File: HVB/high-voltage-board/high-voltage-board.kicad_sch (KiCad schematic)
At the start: 18 parts, among them J1 Conn_01x23, J11 HV-, J2 HECS, J3 HV+, J4 HV-, J5 HV+, J6 HV-, J7 Conn_01x02, J8 HV+, J9 Bender-LV

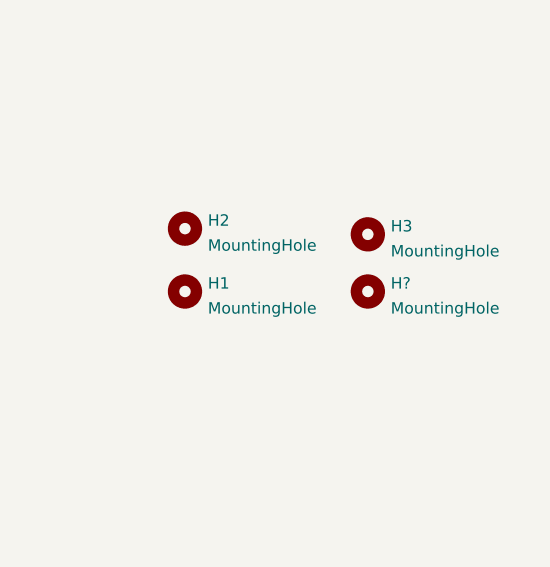
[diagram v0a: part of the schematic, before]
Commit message: adding mounting holes
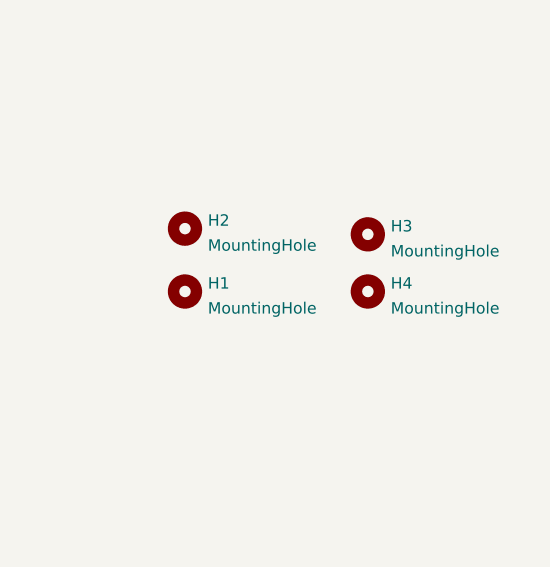
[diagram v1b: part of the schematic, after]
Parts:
- gave numbers to parts that had none: 1
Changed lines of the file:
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@@
   (symbol (lib_id "Mechanical:MountingHole") (at 262.255 162.56 0) (unit 1)
     (in_bom yes) (on_board yes) (fields_autoplaced)
-    (property "Reference" "H?" (id 0) (at 264.795 161.6515 0)
+    (property "Reference" "H4" (id 0) (at 264.795 161.6515 0)
       (effects (font (size 1.27 1.27)) (justify left))
     )
@@
     )
     (path "/245952d0-0e97-4e26-9005-0024054bd321"
-      (reference "H?") (unit 1) (value "MountingHole") (footprint "MountingHole:MountingHole_3.2mm_M3")
+      (reference "H4") (unit 1) (value "MountingHole") (footprint "MountingHole:MountingHole_3.2mm_M3")
     )
     (path "/00000000-0000-0000-0000-00005c830583"

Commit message: updating footprint and 3d model links
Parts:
- J1: footprint AERO_Footprints:TE_1-776087-1 -> AERO_Footprints:TE_1-770669-1_23pin_Horizontal
- J5, J6: footprint Connector_TE-Connectivity:TE_MATE-N-LOK_1-770870-x_1x03_P4.14mm_Vertical -> AERO_Footprints:TE_MATE-N-LOK_1-770870-x_1x03_P4.14mm_Vertical
- J7: footprint Connector_JST:JST_PH_B2B-PH-K_1x02_P2.00mm_Vertical -> Connector_JST:JST_XH_B2B-XH-A_1x02_P2.50mm_Vertical
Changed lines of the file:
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@@
     (property "Reference" "J1" (id 0) (at 23.622 132.9182 0))
     (property "Value" "Conn_01x23" (id 1) (at 23.622 135.2296 0))
-    (property "Footprint" "AERO_Footprints:TE_1-776087-1" (id 2) (at 21.59 166.37 0)
+    (property "Footprint" "AERO_Footprints:TE_1-770669-1_23pin_Horizontal" (id 2) (at 21.59 166.37 0)
       (effects (font (size 1.27 1.27)) hide)
     )
@@
       (effects (font (size 1.27 1.27)) (justify right))
     )
-    (property "Footprint" "Connector_TE-Connectivity:TE_MATE-N-LOK_1-770870-x_1x03_P4.14mm_Vertical" (id 2) (at 45.72 31.75 0)
+    (property "Footprint" "AERO_Footprints:TE_MATE-N-LOK_1-770870-x_1x03_P4.14mm_Vertical" (id 2) (at 45.72 31.75 0)
       (effects (font (size 1.27 1.27)) hide)
     )
@@
     (property "Reference" "J6" (id 0) (at 51.435 48.26 90))
     (property "Value" "HV-" (id 1) (at 52.07 45.72 90))
-    (property "Footprint" "Connector_TE-Connectivity:TE_MATE-N-LOK_1-770870-x_1x03_P4.14mm_Vertical" (id 2) (at 45.72 48.26 0)
+    (property "Footprint" "AERO_Footprints:TE_MATE-N-LOK_1-770870-x_1x03_P4.14mm_Vertical" (id 2) (at 45.72 48.26 0)
       (effects (font (size 1.27 1.27)) hide)
     )
@@
     (property "Reference" "J7" (id 0) (at 67.945 185.8985 0))
     (property "Value" "Conn_01x02" (id 1) (at 67.945 188.6736 0))
-    (property "Footprint" "Connector_JST:JST_PH_B2B-PH-K_1x02_P2.00mm_Vertical" (id 2) (at 67.945 193.675 0)
+    (property "Footprint" "Connector_JST:JST_XH_B2B-XH-A_1x02_P2.50mm_Vertical" (id 2) (at 67.945 193.675 0)
       (effects (font (size 1.27 1.27)) hide)
     )
@@
     )
     (path "/00000000-0000-0000-0000-00005c830583"
-      (reference "J1") (unit 1) (value "Conn_01x23") (footprint "AERO_Footprints:TE_1-776087-1")
+      (reference "J1") (unit 1) (value "Conn_01x23") (footprint "AERO_Footprints:TE_1-770669-1_23pin_Horizontal")
     )
     (path "/00000000-0000-0000-0000-00005c830507"
@@
     )
     (path "/00000000-0000-0000-0000-00005c8305f3"
-      (reference "J5") (unit 1) (value "HV+") (footprint "Connector_TE-Connectivity:TE_MATE-N-LOK_1-770870-x_1x03_P4.14mm_Vertical")
+      (reference "J5") (unit 1) (value "HV+") (footprint "AERO_Footprints:TE_MATE-N-LOK_1-770870-x_1x03_P4.14mm_Vertical")
     )
     (path "/00000000-0000-0000-0000-00005c830602"
-      (reference "J6") (unit 1) (value "HV-") (footprint "Connector_TE-Connectivity:TE_MATE-N-LOK_1-770870-x_1x03_P4.14mm_Vertical")
+      (reference "J6") (unit 1) (value "HV-") (footprint "AERO_Footprints:TE_MATE-N-LOK_1-770870-x_1x03_P4.14mm_Vertical")
     )
     (path "/980ee780-2ccd-48d0-81e9-943616a2d3fc"
-      (reference "J7") (unit 1) (value "Conn_01x02") (footprint "Connector_JST:JST_PH_B2B-PH-K_1x02_P2.00mm_Vertical")
+      (reference "J7") (unit 1) (value "Conn_01x02") (footprint "Connector_JST:JST_XH_B2B-XH-A_1x02_P2.50mm_Vertical")
     )
     (path "/14999d0e-4e0c-4ec9-a7cb-88c272b22a6c"

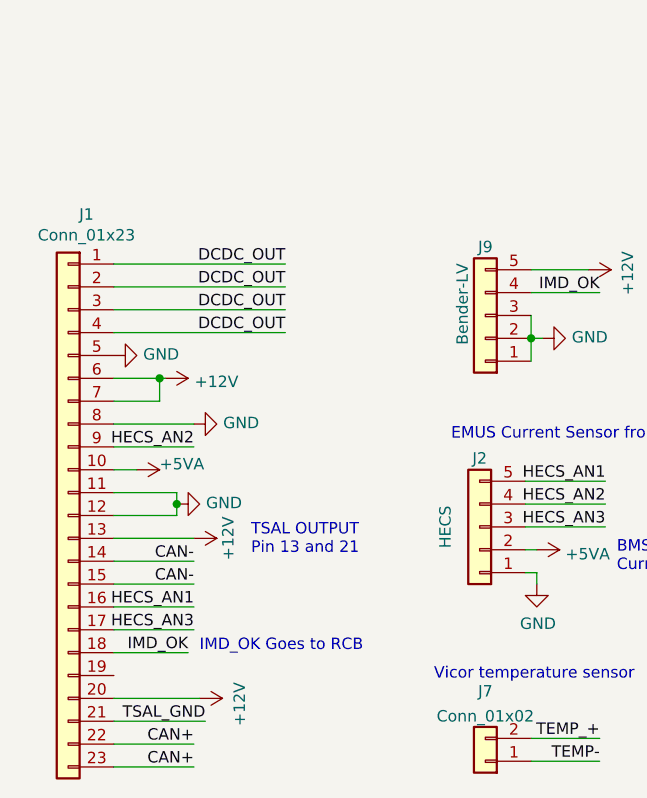
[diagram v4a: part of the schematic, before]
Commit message: updating can pinouts
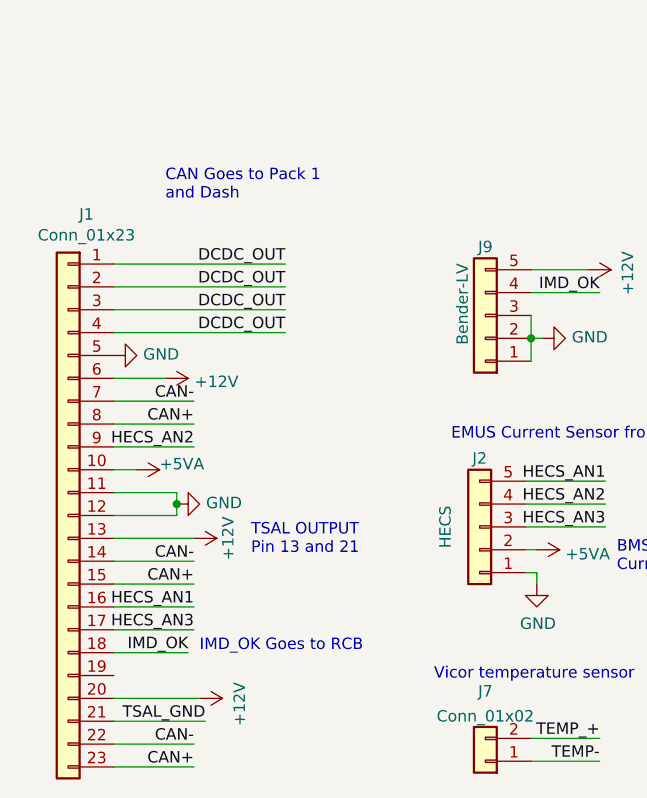
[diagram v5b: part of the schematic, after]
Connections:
- net +12V: no longer J1.7 (Pin_7)
- net CAN+: now also J1.15 (Pin_15), J1.8 (Pin_8); no longer J1.22 (Pin_22)
- net CAN-: now also J1.22 (Pin_22), J1.7 (Pin_7); no longer J1.15 (Pin_15)
- net GND: no longer J1.8 (Pin_8)
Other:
- note added: "CAN Goes to Pack 1 and Dash"
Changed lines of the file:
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@@
   (junction (at 45.72 36.83) (diameter 0) (color 0 0 0 0)
   )
-  (junction (at 31.75 151.13) (diameter 0) (color 0 0 0 0)
-  )
   (junction (at 48.26 43.18) (diameter 0) (color 0 0 0 0)
   )
@@
     (stroke (width 0) (type default) (color 0 0 0 0))
   )
-  (wire (pts (xy 26.67 171.45) (xy 35.56 171.45))
+  (wire (pts (xy 26.67 191.77) (xy 35.56 191.77))
+    (stroke (width 0) (type default) (color 0 0 0 0))
+  )
+  (wire (pts (xy 26.67 153.67) (xy 35.56 153.67))
     (stroke (width 0) (type default) (color 0 0 0 0))
   )
@@
     (stroke (width 0) (type default) (color 0 0 0 0))
   )
-  (wire (pts (xy 26.67 191.77) (xy 35.56 191.77))
+  (wire (pts (xy 26.67 173.99) (xy 35.56 173.99))
     (stroke (width 0) (type default) (color 0 0 0 0))
   )
@@
     (stroke (width 0) (type default) (color 0 0 0 0))
   )
-  (wire (pts (xy 26.67 153.67) (xy 31.75 153.67))
-    (stroke (width 0) (type default) (color 0 0 0 0))
-  )
   (wire (pts (xy 33.655 166.37) (xy 26.67 166.37))
     (stroke (width 0) (type default) (color 0 0 0 0))
@@
     (stroke (width 0) (type default) (color 0 0 0 0))
   )
-  (wire (pts (xy 26.67 173.99) (xy 35.56 173.99))
+  (wire (pts (xy 26.67 171.45) (xy 35.56 171.45))
     (stroke (width 0) (type default) (color 0 0 0 0))
   )
   (wire (pts (xy 26.67 163.83) (xy 33.655 163.83))
+    (stroke (width 0) (type default) (color 0 0 0 0))
+  )
+  (wire (pts (xy 26.67 156.21) (xy 35.56 156.21))
     (stroke (width 0) (type default) (color 0 0 0 0))
   )
@@
     (stroke (width 0) (type default) (color 0 0 0 0))
   )
-  (wire (pts (xy 31.75 153.67) (xy 31.75 151.13))
-    (stroke (width 0) (type default) (color 0 0 0 0))
-  )
   (wire (pts (xy 147.32 91.44) (xy 162.56 91.44))
     (stroke (width 0) (type default) (color 0 0 0 0))
@@
     (stroke (width 0) (type default) (color 0 0 0 0))
   )
-  (wire (pts (xy 31.75 151.13) (xy 32.385 151.13))
+  (wire (pts (xy 26.67 151.13) (xy 32.385 151.13))
     (stroke (width 0) (type default) (color 0 0 0 0))
   )
@@
     (stroke (width 0) (type default) (color 0 0 0 0))
   )
-  (wire (pts (xy 35.56 156.21) (xy 26.67 156.21))
-    (stroke (width 0) (type default) (color 0 0 0 0))
-  )
   (wire (pts (xy 48.26 36.83) (xy 62.23 36.83))
     (stroke (width 0) (type default) (color 0 0 0 0))
@@
     (stroke (width 0) (type default) (color 0 0 0 0))
   )
-  (wire (pts (xy 26.67 151.13) (xy 31.75 151.13))
-    (stroke (width 0) (type default) (color 0 0 0 0))
-  )
   (wire (pts (xy 26.67 143.51) (xy 45.72 143.51))
     (stroke (width 0) (type default) (color 0 0 0 0))
@@
   )
   (text "EMUS Current Sensor from BMS" (at 64.135 158.115 0)
+    (effects (font (size 1.27 1.27)) (justify left bottom))
+  )
+  (text "CAN Goes to Pack 1\nand Dash" (at 32.385 131.445 0)
     (effects (font (size 1.27 1.27)) (justify left bottom))
   )
@@
     (effects (font (size 1.27 1.27)) (justify left bottom))
   )
+  (label "CAN-" (at 35.56 153.67 180)
+    (effects (font (size 1.27 1.27)) (justify right bottom))
+  )
   (label "IMD_OK" (at 80.645 141.605 180)
     (effects (font (size 1.27 1.27)) (justify right bottom))
   )
-  (label "CAN-" (at 35.56 173.99 180)
+  (label "CAN-" (at 35.56 171.45 180)
+    (effects (font (size 1.27 1.27)) (justify right bottom))
+  )
+  (label "CAN+" (at 35.56 156.21 180)
     (effects (font (size 1.27 1.27)) (justify right bottom))
   )
@@
     (effects (font (size 1.27 1.27)) (justify right bottom))
   )
-  (label "CAN+" (at 35.56 191.77 180)
+  (label "CAN+" (at 35.56 173.99 180)
     (effects (font (size 1.27 1.27)) (justify right bottom))
   )
@@
     (effects (font (size 1.27 1.27)) (justify left bottom))
   )
-  (label "CAN-" (at 35.56 171.45 180)
+  (label "CAN-" (at 35.56 191.77 180)
     (effects (font (size 1.27 1.27)) (justify right bottom))
   )
@@
     (pin "2")
   )
-  (symbol (lib_id "power:GND") (at 35.56 156.21 90) (unit 1)
-    (in_bom yes) (on_board yes)
-    (property "Reference" "#PWR0108" (id 0) (at 41.91 156.21 0)
-      (effects (font (size 1.27 1.27)) hide)
-    )
-    (property "Value" "GND" (id 1) (at 38.8112 156.083 90)
-      (effects (font (size 1.27 1.27)) (justify right))
-    )
-    (property "Footprint" "" (id 2) (at 35.56 156.21 0)
-      (effects (font (size 1.27 1.27)) hide)
-    )
-    (property "Datasheet" "" (id 3) (at 35.56 156.21 0)
-      (effects (font (size 1.27 1.27)) hide)
-    )
-    (pin "1")
-  )
   (symbol (lib_id "power:GND") (at 26.67 148.59 90) (unit 1)
     (in_bom yes) (on_board yes)
@@
       (reference "#PWR0107") (unit 1) (value "+12V") (footprint "")
     )
-    (path "/79cdd589-0e2f-43a0-b8f3-7a47a6bac649"
-      (reference "#PWR0108") (unit 1) (value "GND") (footprint "")
-    )
     (path "/00000000-0000-0000-0000-00005c8304a7/68f92a54-f14a-4338-bfb4-429506e9b675"

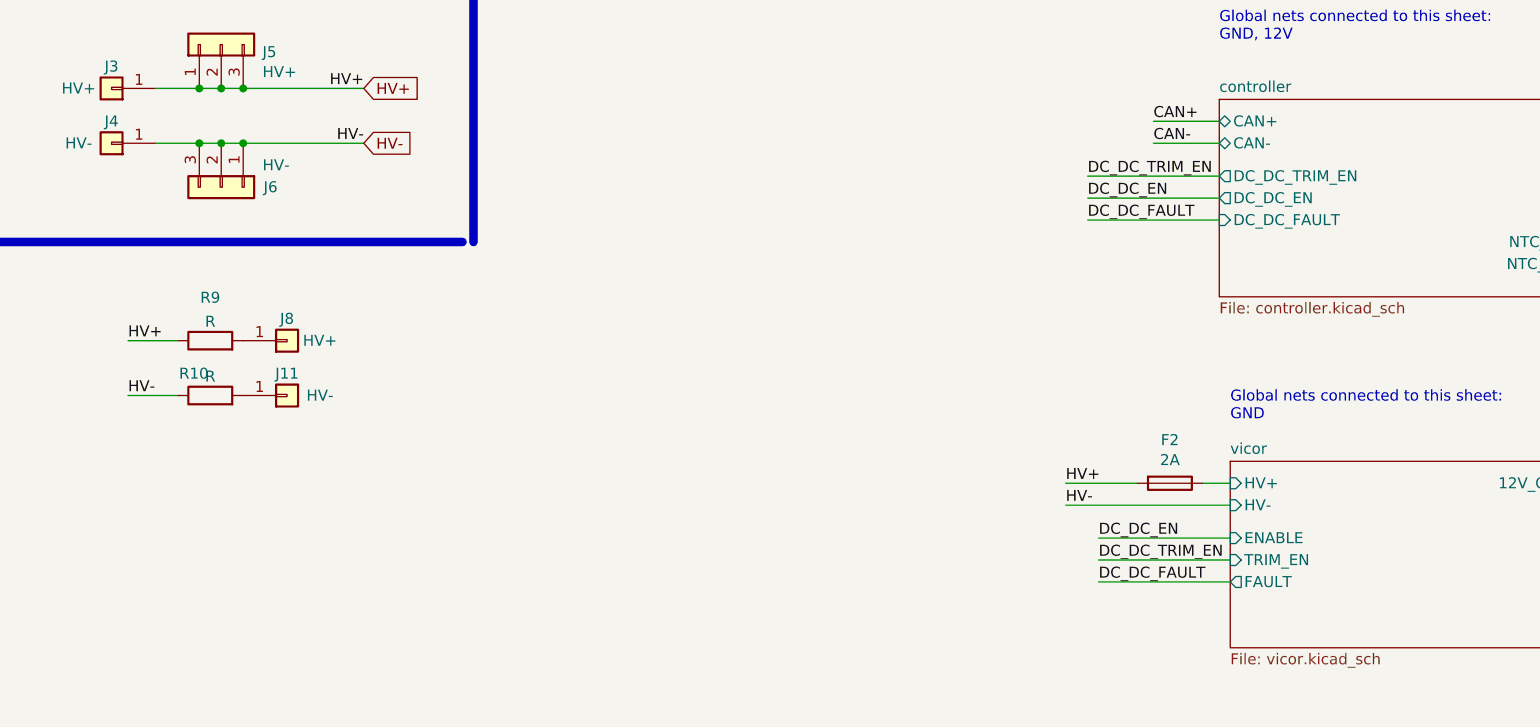
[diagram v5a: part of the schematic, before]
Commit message: Major Review and Part Update
updating footprints, component values, layouts
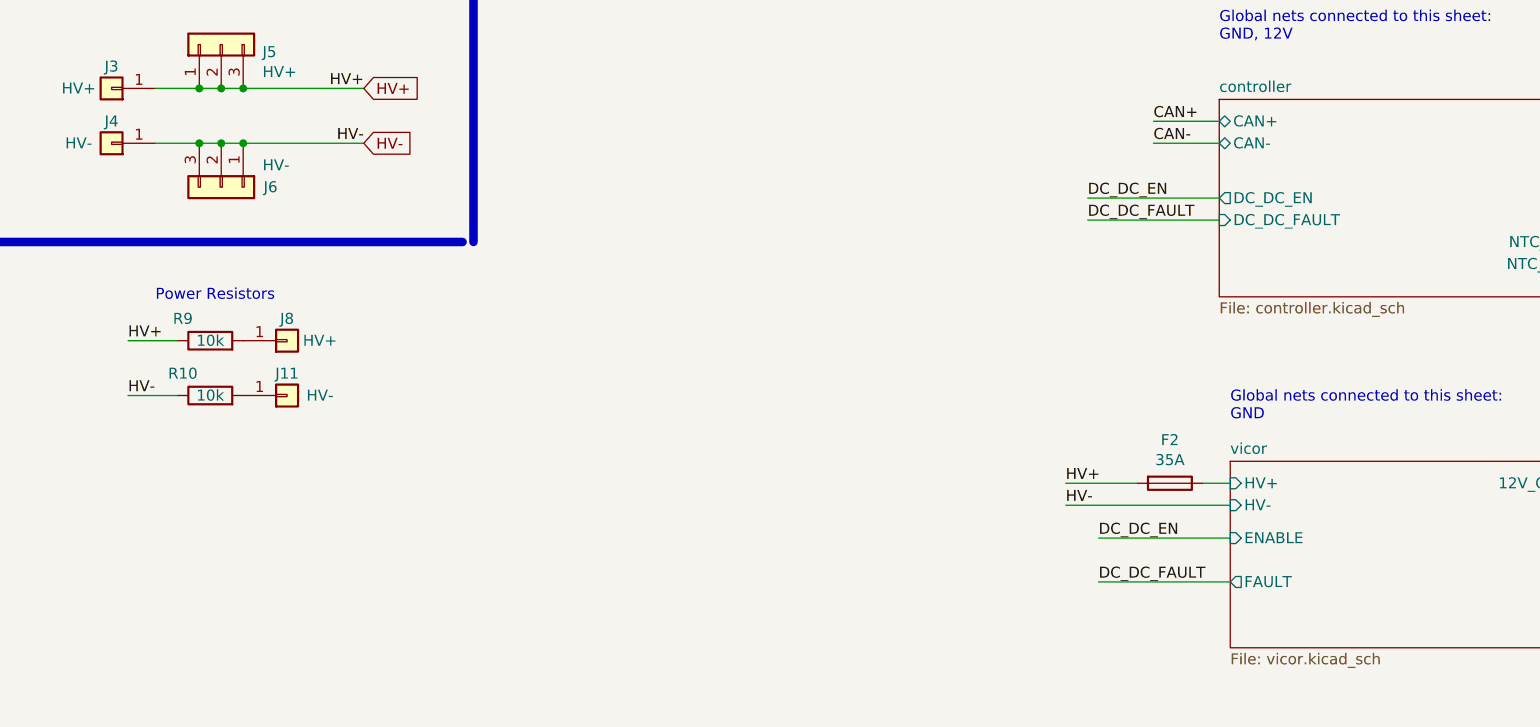
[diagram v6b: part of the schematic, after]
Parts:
- F2: value 2A -> 35A
- R10, R9: value R -> 10k; footprint Resistor_THT:R_Axial_Power_L38.0mm_W9.0mm_P45.72mm -> Resistor_THT:R_Axial_Power_L50.0mm_W9.0mm_P60.96mm
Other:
- sheet controller ports: added none; removed DC_DC_TRIM_EN
- sheet vicor ports: added none; removed TRIM_EN
- note added: "Power Resistors"
